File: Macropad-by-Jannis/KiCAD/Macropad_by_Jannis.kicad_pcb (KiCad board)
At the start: 2 copper layers, 42.9 x 62.9 mm, 7 parts, among them SW1 SW_Push, SW2 SW_Push, SW3 SW_Push, SW4 SW_Push, U1 XIAO-RP2040-DIP

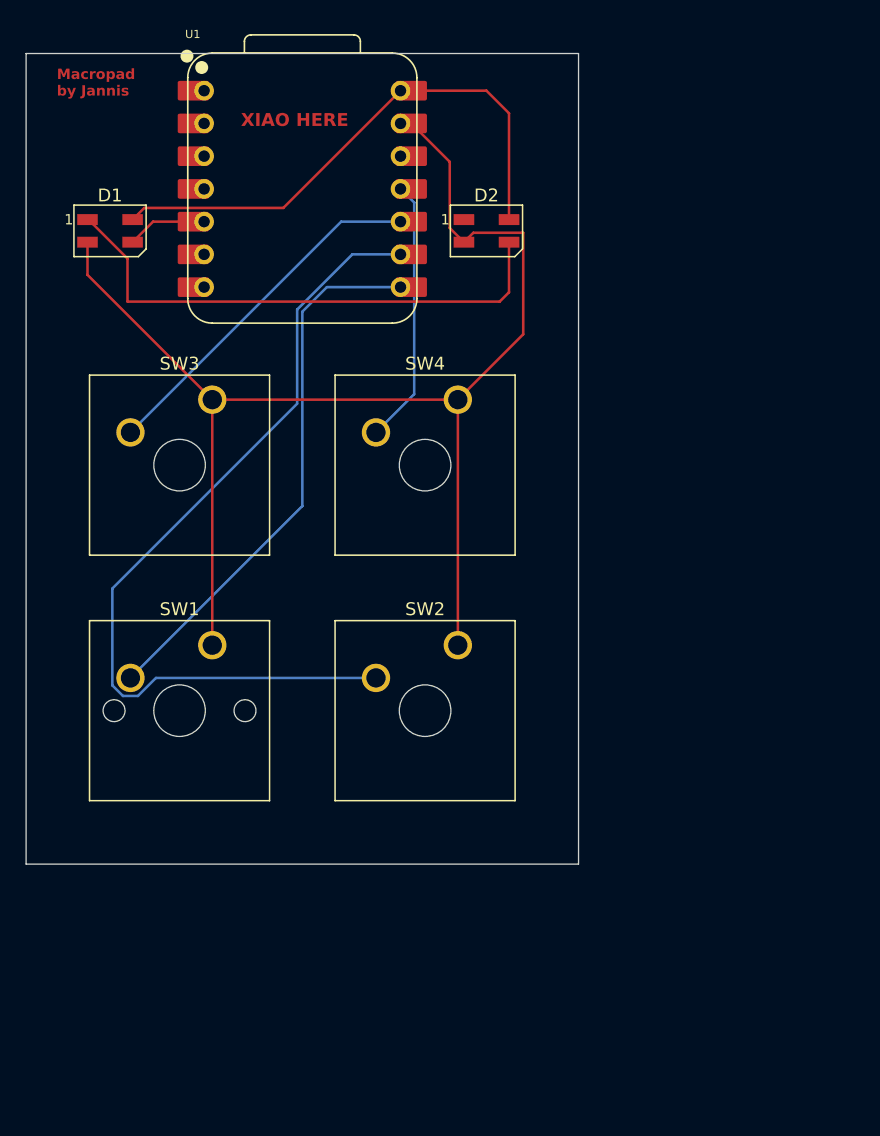
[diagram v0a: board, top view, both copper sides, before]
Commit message: 3 reihen
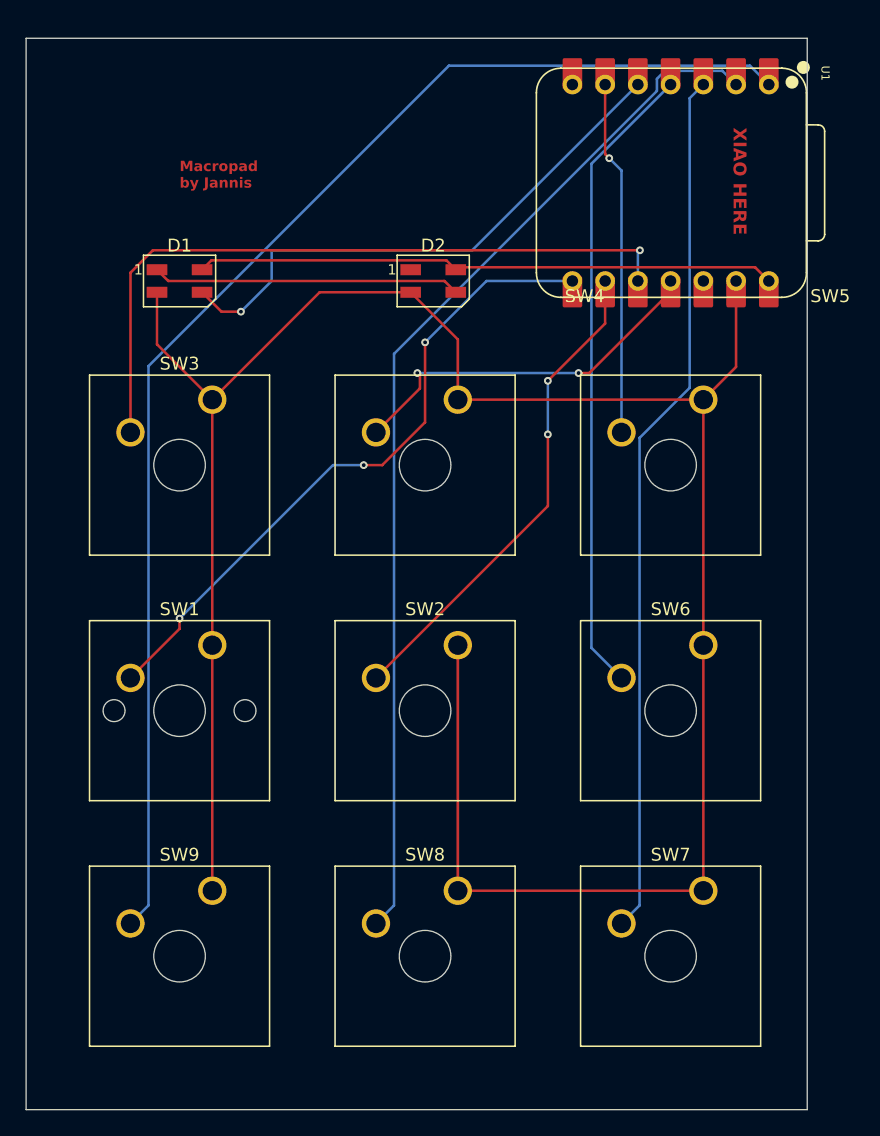
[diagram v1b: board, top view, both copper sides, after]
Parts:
- added SW5: SW_Push, Button_Switch_Keyboard:SW_Cherry_MX_1.00u_Plate, F.Cu at (178.8, 78.3)
- added SW6: SW_Push, Button_Switch_Keyboard:SW_Cherry_MX_1.00u_Plate, F.Cu at (178.8, 97.3)
- added SW7: SW_Push, Button_Switch_Keyboard:SW_Cherry_MX_1.00u_Plate, F.Cu at (178.8, 116.4)
- added SW8: SW_Push, Button_Switch_Keyboard:SW_Cherry_MX_1.00u_Plate, F.Cu at (159.7, 116.4)
- added SW9: SW_Push, Button_Switch_Keyboard:SW_Cherry_MX_1.00u_Plate, F.Cu at (140.7, 116.4)
- moved U1 28.6 mm to (176.2, 61.4), turned to -90 degrees
- moved D1 6.65 mm to (138.1, 69.1)
- moved D2 5.67 mm to (157.8, 69.1)
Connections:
- U1 pad 1: unconnected-(U1-GPIO26/ADC0/A0-Pad1) -> Net-(U1-GPIO26/ADC0/A0)
- U1 pad 2: unconnected-(U1-GPIO27/ADC1/A1-Pad2) -> Net-(U1-GPIO27/ADC1/A1)
- U1 pad 3: unconnected-(U1-GPIO28/ADC2/A2-Pad3) -> Net-(U1-GPIO28/ADC2/A2)
- U1 pad 4: unconnected-(U1-GPIO29/ADC3/A3-Pad4) -> Net-(U1-GPIO29/ADC3/A3)
- U1 pad 6: unconnected-(U1-GPIO7/SCL-Pad6) -> Net-(U1-GPIO7/SCL)
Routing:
- net Net-(U1-GPIO26/ADC0/A0): track 0.00 -> 102.2 mm
- net Net-(U1-GPIO27/ADC1/A1): track 0.00 -> 81.4 mm
- net GND: track 104.2 -> 182.4 mm
- net Net-(U1-GPIO28/ADC2/A2): track 0.00 -> 67.7 mm
- net Net-(U1-GPIO29/ADC3/A3): track 0.00 -> 49.5 mm
- net Net-(D1-DIN): track 6.21 -> 43.1 mm, vias 0 -> 1
- net Net-(U1-GPIO2/SCK): track 66.3 -> 37.3 mm, vias 0 -> 2
- net Net-(U1-GPIO7/SCL): track 0.00 -> 27.5 mm, vias 0 -> 1
- net Net-(U1-GPIO4/MISO): track 27.7 -> 55.1 mm, vias 0 -> 1
- net Net-(D1-DOUT): track 41.5 -> 24.0 mm
- net Net-(U1-GPIO1/RX): track 42.3 -> 51.1 mm, vias 0 -> 3
- net Net-(U1-GPIO3/MOSI): track 20.6 -> 28.5 mm, vias 0 -> 2
- net +5V: track 41.5 -> 45.1 mm
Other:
- board size 42.9 x 62.9 mm -> 60.6 x 83.1 mm
